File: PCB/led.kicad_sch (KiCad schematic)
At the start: 200 parts

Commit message: LED Diode Placement finished
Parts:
- C10, C100, C101, C102, C103, C104, C105, C106, C107, C108, C11, C12, C13, C14, C15, C16, C17, C18, C19, C20, C21, C22, C23, C24, C25, C26, C27, C28, C29, C30, C31, C32, C33, C34, C35, C36, C37, C38, C39, C40, C41, C42, C43, C44, C45, C46, C47, C48, C49, C50, C51, C52, C53, C54, C55, C56, C57, C58, C59, C60, C61, C62, C63, C64, C65, C66, C67, C68, C69, C70, C71, C72, C73, C74, C75, C76, C77, C78, C79, C80, C81, C82, C83, C84, C85, C86, C87, C88, C89, C9, C90, C91, C92, C93, C94, C95, C96, C97, C98, C99: footprint Capacitor_SMD:C_0805_2012Metric -> (none)

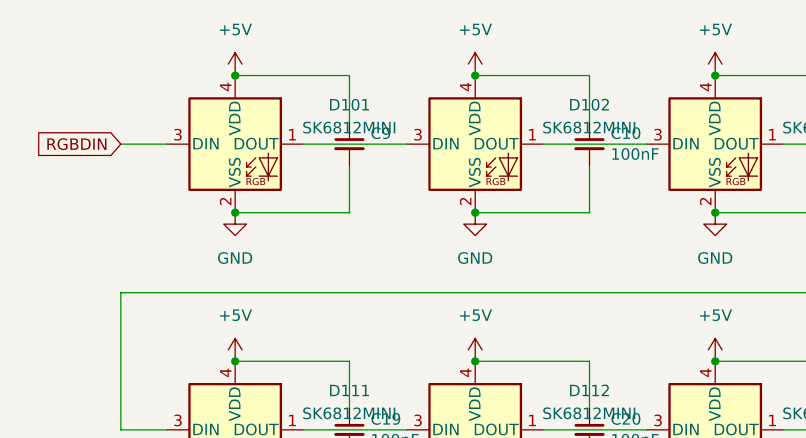
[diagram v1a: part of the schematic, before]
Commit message: LED +5 Wired, COL and ROW Buses nearly finished
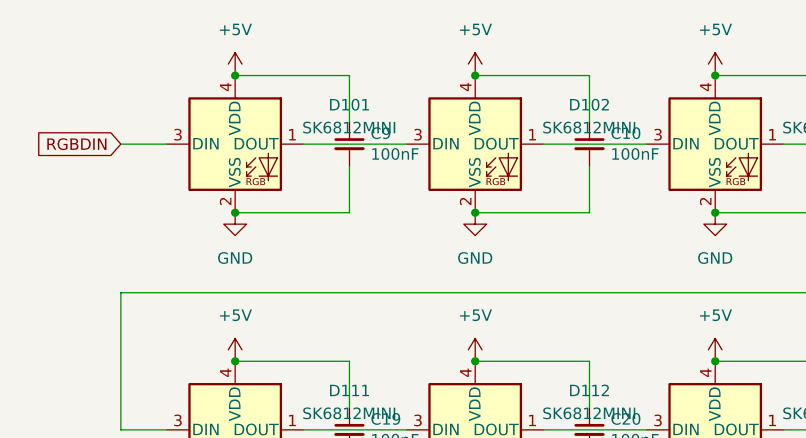
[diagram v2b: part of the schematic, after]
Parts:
- C10, C100, C101, C102, C103, C104, C105, C106, C107, C108, C11, C12, C13, C14, C15, C16, C17, C18, C19, C20, C21, C22, C23, C24, C25, C26, C27, C28, C29, C30, C31, C32, C33, C34, C35, C36, C37, C38, C39, C40, C41, C42, C43, C44, C45, C46, C47, C48, C49, C50, C51, C52, C53, C54, C55, C56, C57, C58, C59, C60, C61, C62, C63, C64, C65, C66, C67, C68, C69, C70, C71, C72, C73, C74, C75, C76, C77, C78, C79, C80, C81, C82, C83, C84, C85, C86, C87, C88, C89, C90, C91, C92, C93, C94, C95, C96, C97, C98, C99: footprint (none) -> led:led_capacitor
- C9: value (none) -> 100nF; footprint (none) -> led:led_capacitor

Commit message: datalines and mosfet
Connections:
- net +5V: no longer C10.1, C11.1, C12.1, C13.1, C14.1, C15.1, C16.1, C17.1, C18.1, C9.1, D101.4 (VDD), D102.4 (VDD), D103.4 (VDD), D104.4 (VDD), D105.4 (VDD), D106.4 (VDD), D107.4 (VDD), D108.4 (VDD), D109.4 (VDD), D110.4 (VDD)
- new net led_5V: C10.1, C11.1, C12.1, C13.1, C14.1, C15.1, C16.1, C17.1, C18.1, C9.1, D101.4 (VDD), D102.4 (VDD), D103.4 (VDD), D104.4 (VDD), D105.4 (VDD), D106.4 (VDD), D107.4 (VDD), D108.4 (VDD), D109.4 (VDD), D110.4 (VDD)

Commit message: Relocated JST Connector
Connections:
- net +5V is gone; now on net led_5V: C100.1, C101.1, C102.1, C103.1, C104.1, C105.1, C106.1, C107.1, C108.1, C19.1, C20.1, C21.1, C22.1, C23.1, C24.1, C25.1, C26.1, C27.1, C28.1, C29.1, C30.1, C31.1, C32.1, C33.1, C34.1, C35.1, C36.1, C37.1, C38.1, C39.1, C40.1, C41.1, C42.1, C43.1, C44.1, C45.1, C46.1, C47.1, C48.1, C49.1, C50.1, C51.1, C52.1, C53.1, C54.1, C55.1, C56.1, C57.1, C58.1, C59.1, C60.1, C61.1, C62.1, C63.1, C64.1, C65.1, C66.1, C67.1, C68.1, C69.1, C70.1, C71.1, C72.1, C73.1, C74.1, C75.1, C76.1, C77.1, C78.1, C79.1, C80.1, C81.1, C82.1, C83.1, C84.1, C85.1, C86.1, C87.1, C88.1, C89.1, C90.1, C91.1, C92.1, C93.1, C94.1, C95.1, C96.1, C97.1, C98.1, C99.1, D111.4 (VDD), D112.4 (VDD), D113.4 (VDD), D114.4 (VDD), D115.4 (VDD), D116.4 (VDD), D117.4 (VDD), D118.4 (VDD), D119.4 (VDD), D120.4 (VDD), D121.4 (VDD), D122.4 (VDD), D123.4 (VDD), D124.4 (VDD), D125.4 (VDD), D126.4 (VDD), D127.4 (VDD), D128.4 (VDD), D129.4 (VDD), D130.4 (VDD), D131.4 (VDD), D132.4 (VDD), D133.4 (VDD), D134.4 (VDD), D135.4 (VDD), D136.4 (VDD), D137.4 (VDD), D138.4 (VDD), D139.4 (VDD), D140.4 (VDD), D141.4 (VDD), D142.4 (VDD), D143.4 (VDD), D144.4 (VDD), D145.4 (VDD), D146.4 (VDD), D147.4 (VDD), D148.4 (VDD), D149.4 (VDD), D150.4 (VDD), D151.4 (VDD), D152.4 (VDD), D153.4 (VDD), D154.4 (VDD), D155.4 (VDD), D156.4 (VDD), D157.4 (VDD), D158.4 (VDD), D159.4 (VDD), D160.4 (VDD), D161.4 (VDD), D162.4 (VDD), D163.4 (VDD), D164.4 (VDD), D165.4 (VDD), D166.4 (VDD), D167.4 (VDD), D168.4 (VDD), D169.4 (VDD), D170.4 (VDD), D171.4 (VDD), D172.4 (VDD), D173.4 (VDD), D174.4 (VDD), D175.4 (VDD), D176.4 (VDD), D177.4 (VDD), D178.4 (VDD), D179.4 (VDD), D180.4 (VDD), D181.4 (VDD), D182.4 (VDD), D183.4 (VDD), D184.4 (VDD), D185.4 (VDD), D186.4 (VDD), D187.4 (VDD), D188.4 (VDD), D189.4 (VDD), D190.4 (VDD), D191.4 (VDD), D192.4 (VDD), D193.4 (VDD), D194.4 (VDD), D195.4 (VDD), D196.4 (VDD), D197.4 (VDD), D198.4 (VDD), D199.4 (VDD), D200.4 (VDD)

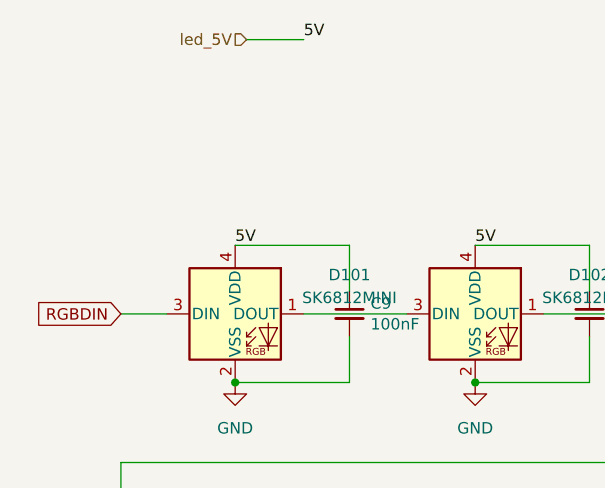
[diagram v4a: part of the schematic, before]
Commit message: change port position
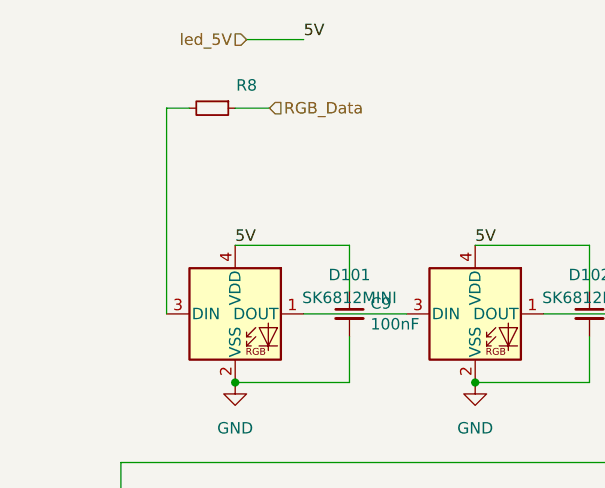
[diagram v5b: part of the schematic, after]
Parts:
- added R8: (no value), symbol Device:R_Small
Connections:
- net RGBDIN: no longer names the net of D101.3 (DIN)
- net RGBDIN: now also R8.2
- new net RGB_Data: R8.1
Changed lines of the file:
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@@
     (stroke (width 0) (type default) (color 0 0 0 0))
   )
+  (wire (pts (xy 17.78 59.69) (xy 17.78 36.83))
+    (stroke (width 0) (type default) (color 0 0 0 0))
+  )
   (wire (pts (xy 144.78 147.32) (xy 144.78 152.4))
     (stroke (width 0) (type default) (color 0 0 0 0))
@@
     (stroke (width 0) (type default) (color 0 0 0 0))
   )
-  (wire (pts (xy 12.7 59.69) (xy 17.78 59.69))
-    (stroke (width 0) (type default) (color 0 0 0 0))
-  )
   (wire (pts (xy 25.4 321.31) (xy 38.1 321.31))
     (stroke (width 0) (type default) (color 0 0 0 0))
@@
     (stroke (width 0) (type default) (color 0 0 0 0))
   )
+  (wire (pts (xy 25.4 36.83) (xy 29.21 36.83))
+    (stroke (width 0) (type default) (color 0 0 0 0))
+  )
   (wire (pts (xy 273.05 218.44) (xy 284.48 218.44))
     (stroke (width 0) (type default) (color 0 0 0 0))
@@
     (stroke (width 0) (type default) (color 0 0 0 0))
   )
+  (wire (pts (xy 17.78 36.83) (xy 20.32 36.83))
+    (stroke (width 0) (type default) (color 0 0 0 0))
+  )
   (wire (pts (xy 118.11 52.07) (xy 118.11 57.15))
     (stroke (width 0) (type default) (color 0 0 0 0))
@@
     (effects (font (size 1.27 1.27)) (justify left bottom))
   )
-  (global_label "RGBDIN" (shape input) (at 12.7 59.69 180) (fields_autoplaced)
-    (effects (font (size 1.27 1.27)) (justify right))
-    (property "Intersheet References" "${INTERSHEET_REFS}" (id 0) (at 3.3606 59.6106 0)
-      (effects (font (size 1.27 1.27)) (justify right) hide)
-    )
-  )
   (hierarchical_label "led_5V" (shape input) (at 26.67 29.21 180)
     (effects (font (size 1.27 1.27)) (justify right))
   )
+  (hierarchical_label "RGB_Data" (shape input) (at 29.21 36.83 0)
+    (effects (font (size 1.27 1.27)) (justify left))
+  )
   (symbol (lib_id "power:GND") (at 25.4 289.56 0) (unit 1)
     (in_bom yes) (on_board yes) (fields_autoplaced)
@@
     (pin "1")
   )
+  (symbol (lib_id "Device:R_Small") (at 22.86 36.83 270) (unit 1)
+    (in_bom yes) (on_board yes)
+    (property "Reference" "R8" (id 0) (at 26.67 34.29 90))
+    (property "Value" "" (id 1) (at 22.86 34.163 90))
+    (property "Footprint" "" (id 2) (at 22.86 36.83 0)
+      (effects (font (size 1.27 1.27)) hide)
+    )
+    (property "Datasheet" "~" (id 3) (at 22.86 36.83 0)
+      (effects (font (size 1.27 1.27)) hide)
+    )
+    (pin "1")
+    (pin "2")
+  )
   (symbol (lib_id "Device:C_Small") (at 118.11 123.19 0) (unit 1)

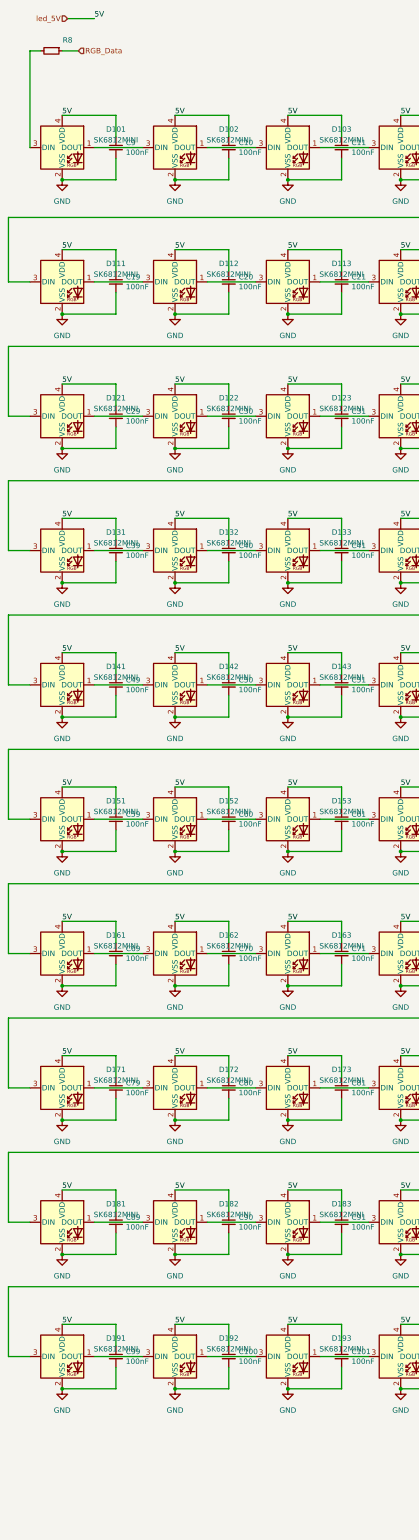
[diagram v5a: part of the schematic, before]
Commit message: changes:\n\n -change zones\n -add mounting holes\n -change via size
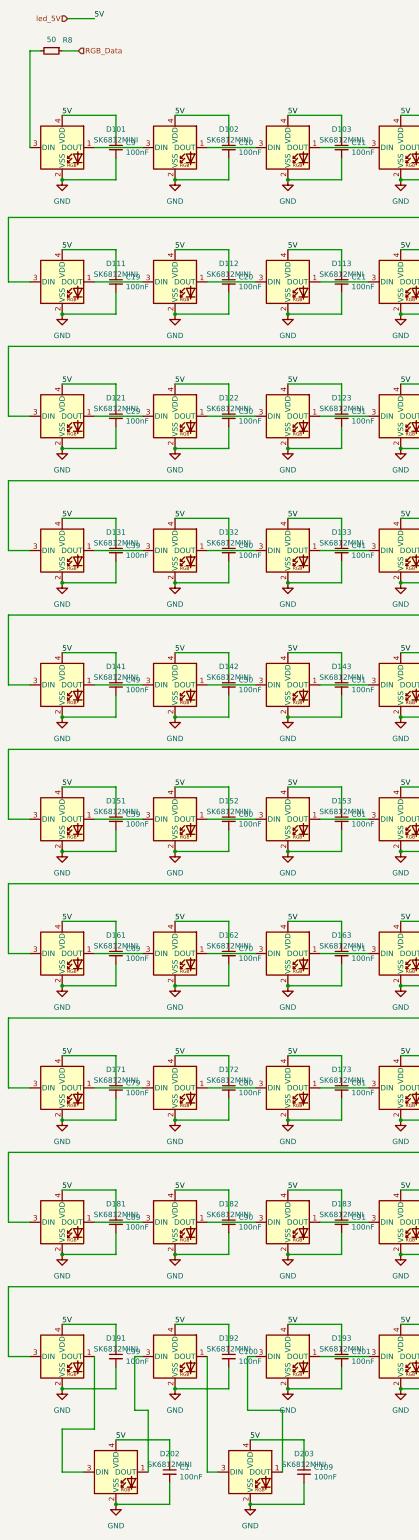
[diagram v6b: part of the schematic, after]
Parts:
- added C1, C109: 100nF, led:led_capacitor, symbol Device:C_Small
- added D202, D203: SK6812MINI, led:SK6812MINI_3.5x3.7mm_SMD-Flipped-Back, symbol LED:SK6812MINI
- R8: value (none) -> 50; footprint (none) -> Resistor_SMD:R_0805_2012Metric
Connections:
- net GND: now also C1.2, C109.2, D202.2 (VSS), D203.2 (VSS)
- net led_5V: now also C1.1, C109.1, D202.4 (VDD), D203.4 (VDD)
- net at D193.3 (DIN): now also D203.1 (DOUT); no longer D192.1 (DOUT)
- net at D192.3 (DIN): now also D202.1 (DOUT); no longer D191.1 (DOUT)
- new net: D192.1 (DOUT), D203.3 (DIN)
- new net: D191.1 (DOUT), D202.3 (DIN)

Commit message: production?
still hope
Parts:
- C1, C10, C100, C101, C102, C103, C104, C105, C106, C107, C108, C109, C11, C12, C13, C14, C15, C16, C17, C18, C19, C20, C21, C22, C23, C24, C25, C26, C27, C28, C29, C30, C31, C32, C33, C34, C35, C36, C37, C38, C39, C40, C41, C42, C43, C44, C45, C46, C47, C48, C49, C50, C51, C52, C53, C54, C55, C56, C57, C58, C59, C60, C61, C62, C63, C64, C65, C66, C67, C68, C69, C70, C71, C72, C73, C74, C75, C76, C77, C78, C79, C80, C81, C82, C83, C84, C85, C86, C87, C88, C89, C9, C90, C91, C92, C93, C94, C95, C96, C97, C98, C99: LCSC Part (none) -> C476766
- D101, D102, D103, D104, D105, D106, D107, D108, D109, D110, D111, D112, D113, D114, D115, D116, D117, D118, D119, D120, D121, D122, D123, D124, D125, D126, D127, D128, D129, D130, D131, D132, D133, D134, D135, D136, D137, D138, D139, D140, D141, D142, D143, D144, D145, D146, D147, D148, D149, D150, D151, D152, D153, D154, D155, D156, D157, D158, D159, D160, D161, D162, D163, D164, D165, D166, D167, D168, D169, D170, D171, D172, D173, D174, D175, D176, D177, D178, D179, D180, D181, D182, D183, D184, D185, D186, D187, D188, D189, D190, D191, D192, D193, D194, D195, D196, D197, D198, D199, D200, D202, D203: footprint led:SK6812MINI_3.5x3.7mm_SMD-Flipped-Back -> (none)

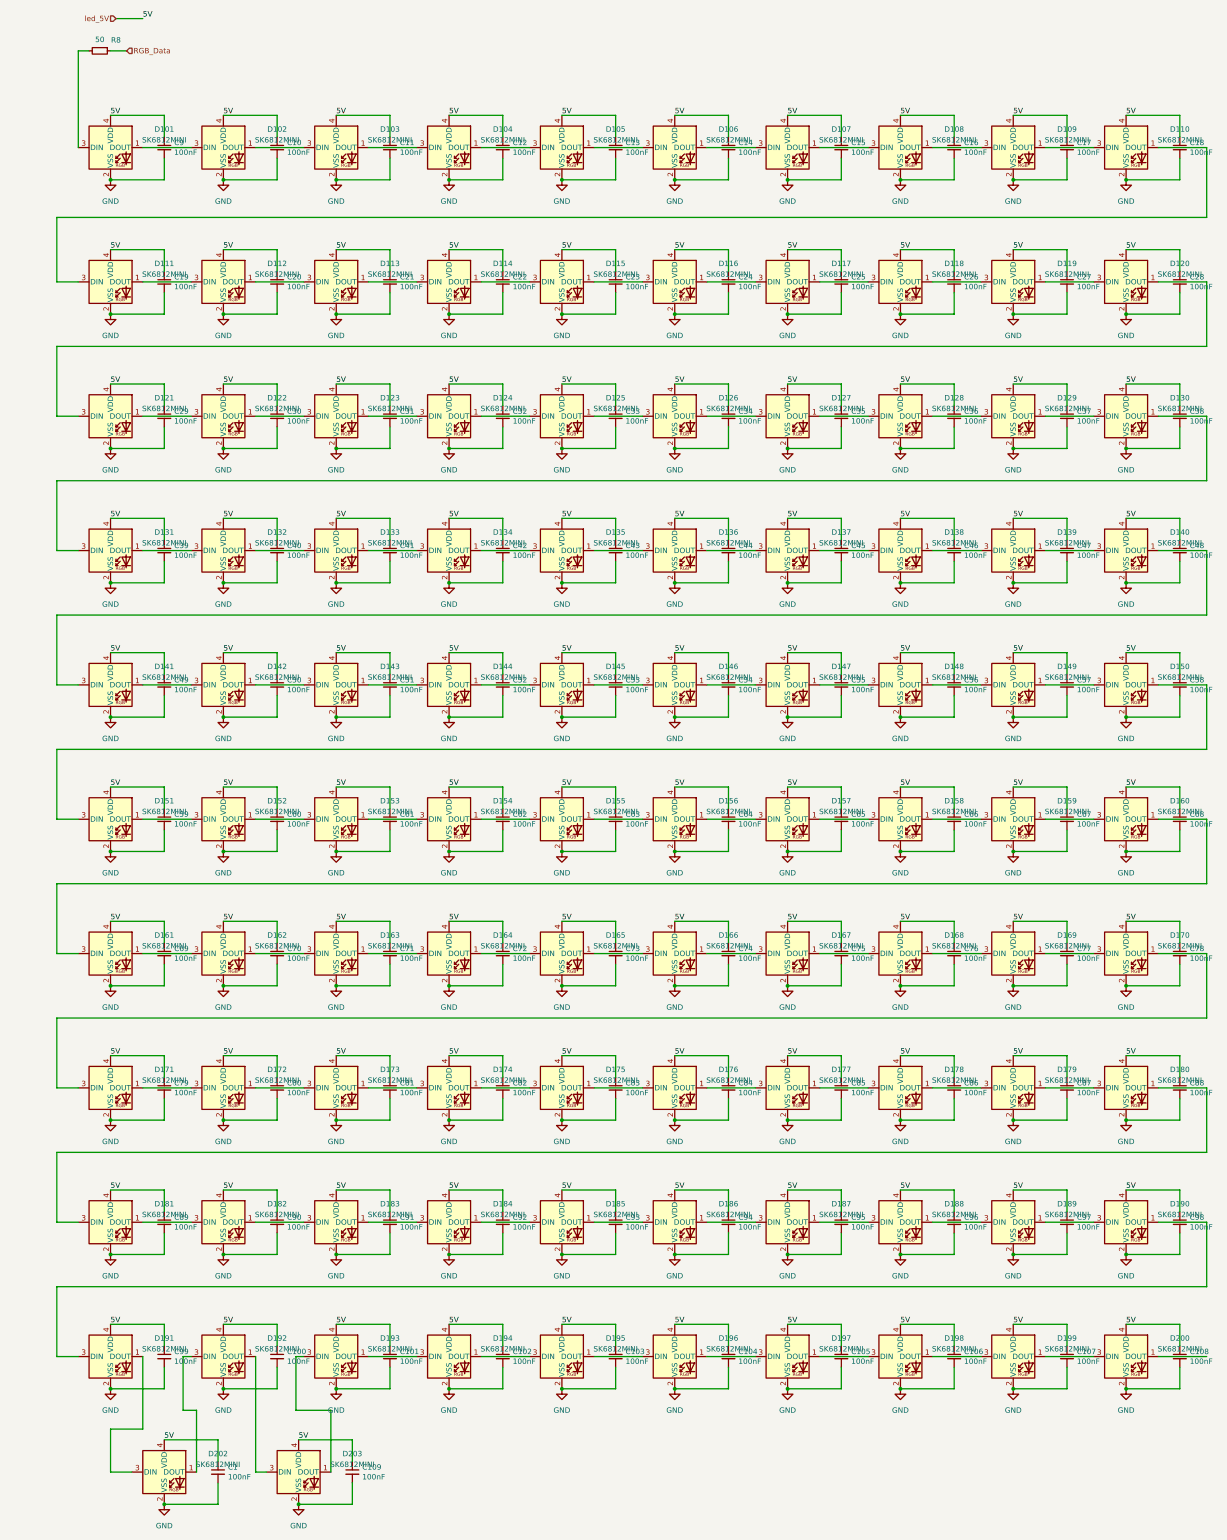
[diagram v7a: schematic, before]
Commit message: Fixed LEDs
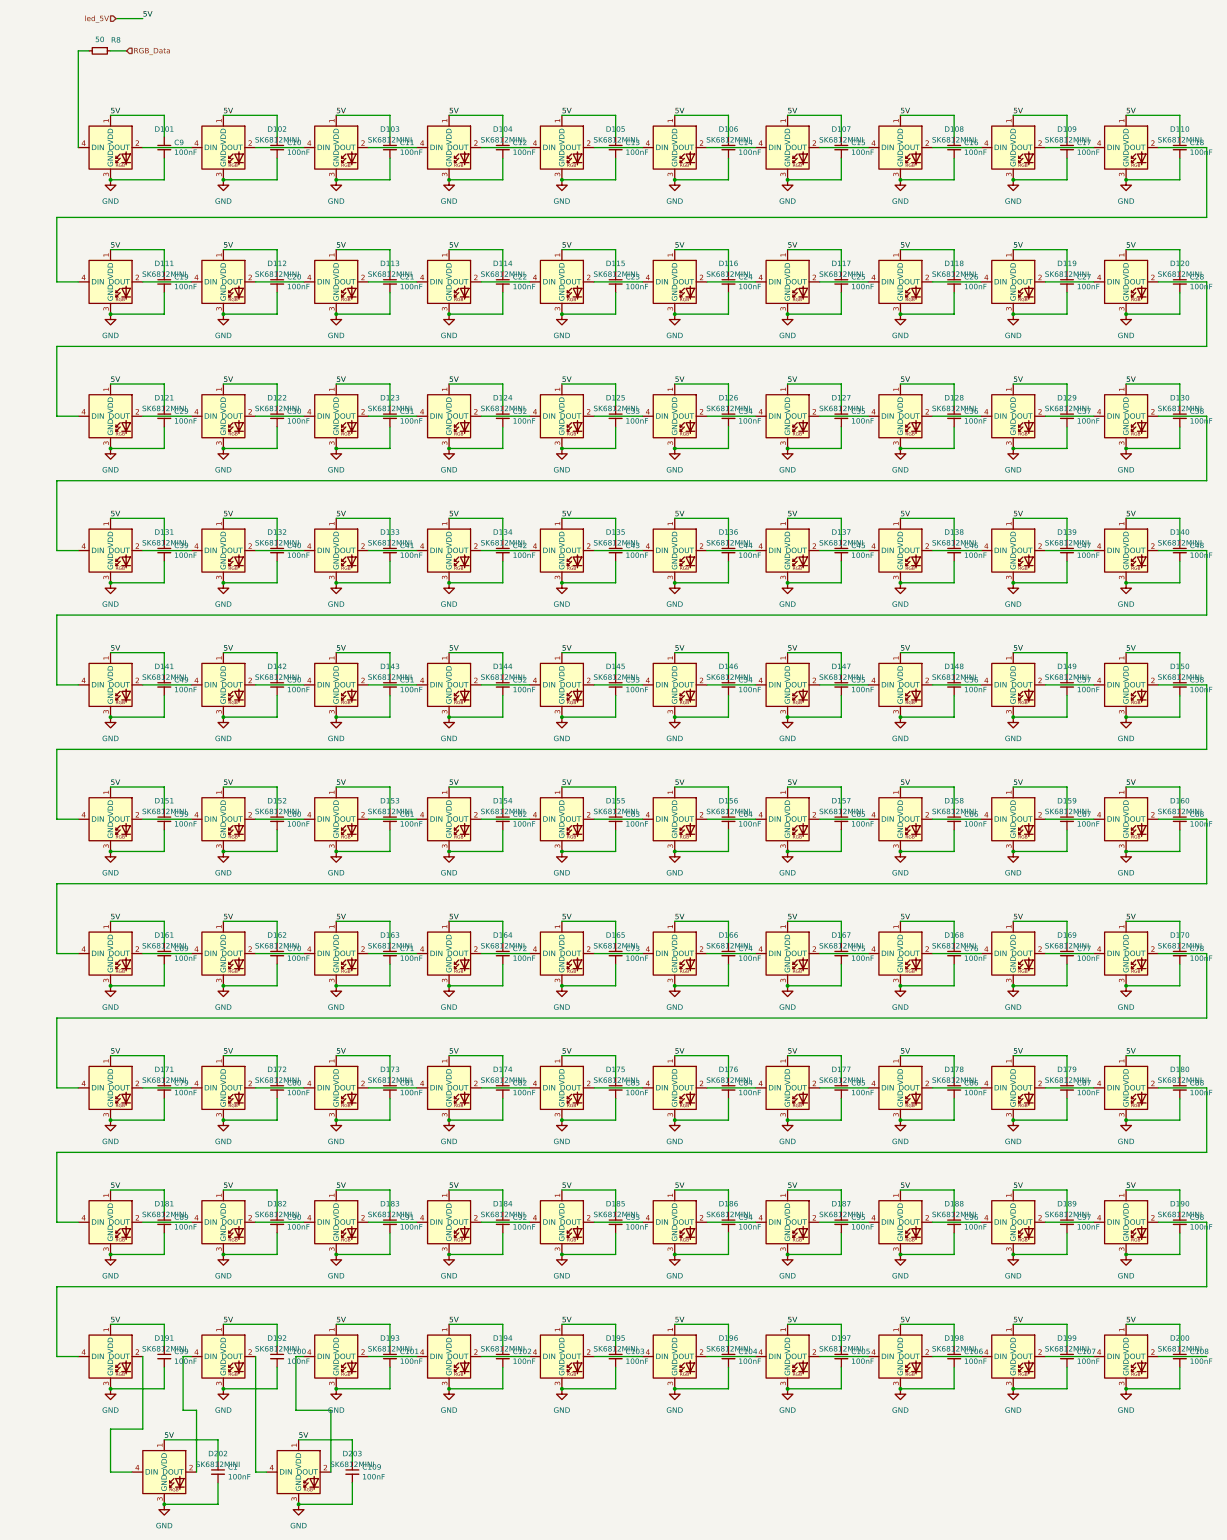
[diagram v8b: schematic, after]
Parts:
- D101: value SK6812MINI -> (none); symbol LED:SK6812MINI -> randomSymbols:SK6812MINI-E
- D102, D103, D104, D105, D106, D107, D108, D109, D110, D111, D112, D113, D114, D115, D116, D117, D118, D119, D120, D121, D122, D123, D124, D125, D126, D127, D128, D129, D130, D131, D132, D133, D134, D135, D136, D137, D138, D139, D140, D141, D142, D143, D144, D145, D146, D147, D148, D149, D150, D151, D152, D153, D154, D155, D156, D157, D158, D159, D160, D161, D162, D163, D164, D165, D166, D167, D168, D169, D170, D171, D172, D173, D174, D175, D176, D177, D178, D179, D180, D181, D182, D183, D184, D185, D186, D187, D188, D189, D190, D191, D192, D193, D194, D195, D196, D197, D198, D199, D200, D202, D203: symbol LED:SK6812MINI -> randomSymbols:SK6812MINI-E
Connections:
- net GND: now also D101.3 (GND), D102.3 (GND), D103.3 (GND), D104.3 (GND), D105.3 (GND), D106.3 (GND), D107.3 (GND), D108.3 (GND), D109.3 (GND), D110.3 (GND), D111.3 (GND), D112.3 (GND), D113.3 (GND), D114.3 (GND), D115.3 (GND), D116.3 (GND), D117.3 (GND), D118.3 (GND), D119.3 (GND), D120.3 (GND), D121.3 (GND), D122.3 (GND), D123.3 (GND), D124.3 (GND), D125.3 (GND), D126.3 (GND), D127.3 (GND), D128.3 (GND), D129.3 (GND), D130.3 (GND), D131.3 (GND), D132.3 (GND), D133.3 (GND), D134.3 (GND), D135.3 (GND), D136.3 (GND), D137.3 (GND), D138.3 (GND), D139.3 (GND), D140.3 (GND), D141.3 (GND), D142.3 (GND), D143.3 (GND), D144.3 (GND), D145.3 (GND), D146.3 (GND), D147.3 (GND), D148.3 (GND), D149.3 (GND), D150.3 (GND), D151.3 (GND), D152.3 (GND), D153.3 (GND), D154.3 (GND), D155.3 (GND), D156.3 (GND), D157.3 (GND), D158.3 (GND), D159.3 (GND), D160.3 (GND), D161.3 (GND), D162.3 (GND), D163.3 (GND), D164.3 (GND), D165.3 (GND), D166.3 (GND), D167.3 (GND), D168.3 (GND), D169.3 (GND), D170.3 (GND), D171.3 (GND), D172.3 (GND), D173.3 (GND), D174.3 (GND), D175.3 (GND), D176.3 (GND), D177.3 (GND), D178.3 (GND), D179.3 (GND), D180.3 (GND), D181.3 (GND), D182.3 (GND), D183.3 (GND), D184.3 (GND), D185.3 (GND), D186.3 (GND), D187.3 (GND), D188.3 (GND), D189.3 (GND), D190.3 (GND), D191.3 (GND), D192.3 (GND), D193.3 (GND), D194.3 (GND), D195.3 (GND), D196.3 (GND), D197.3 (GND), D198.3 (GND), D199.3 (GND), D200.3 (GND), D202.3 (GND), D203.3 (GND); no longer D101.2 (VSS), D102.2 (VSS), D103.2 (VSS), D104.2 (VSS), D105.2 (VSS), D106.2 (VSS), D107.2 (VSS), D108.2 (VSS), D109.2 (VSS), D110.2 (VSS), D111.2 (VSS), D112.2 (VSS), D113.2 (VSS), D114.2 (VSS), D115.2 (VSS), D116.2 (VSS), D117.2 (VSS), D118.2 (VSS), D119.2 (VSS), D120.2 (VSS), D121.2 (VSS), D122.2 (VSS), D123.2 (VSS), D124.2 (VSS), D125.2 (VSS), D126.2 (VSS), D127.2 (VSS), D128.2 (VSS), D129.2 (VSS), D130.2 (VSS), D131.2 (VSS), D132.2 (VSS), D133.2 (VSS), D134.2 (VSS), D135.2 (VSS), D136.2 (VSS), D137.2 (VSS), D138.2 (VSS), D139.2 (VSS), D140.2 (VSS), D141.2 (VSS), D142.2 (VSS), D143.2 (VSS), D144.2 (VSS), D145.2 (VSS), D146.2 (VSS), D147.2 (VSS), D148.2 (VSS), D149.2 (VSS), D150.2 (VSS), D151.2 (VSS), D152.2 (VSS), D153.2 (VSS), D154.2 (VSS), D155.2 (VSS), D156.2 (VSS), D157.2 (VSS), D158.2 (VSS), D159.2 (VSS), D160.2 (VSS), D161.2 (VSS), D162.2 (VSS), D163.2 (VSS), D164.2 (VSS), D165.2 (VSS), D166.2 (VSS), D167.2 (VSS), D168.2 (VSS), D169.2 (VSS), D170.2 (VSS), D171.2 (VSS), D172.2 (VSS), D173.2 (VSS), D174.2 (VSS), D175.2 (VSS), D176.2 (VSS), D177.2 (VSS), D178.2 (VSS), D179.2 (VSS), D180.2 (VSS), D181.2 (VSS), D182.2 (VSS), D183.2 (VSS), D184.2 (VSS), D185.2 (VSS), D186.2 (VSS), D187.2 (VSS), D188.2 (VSS), D189.2 (VSS), D190.2 (VSS), D191.2 (VSS), D192.2 (VSS), D193.2 (VSS), D194.2 (VSS), D195.2 (VSS), D196.2 (VSS), D197.2 (VSS), D198.2 (VSS), D199.2 (VSS), D200.2 (VSS), D202.2 (VSS), D203.2 (VSS)
- net led_5V: now also D101.1 (VDD), D102.1 (VDD), D103.1 (VDD), D104.1 (VDD), D105.1 (VDD), D106.1 (VDD), D107.1 (VDD), D108.1 (VDD), D109.1 (VDD), D110.1 (VDD), D111.1 (VDD), D112.1 (VDD), D113.1 (VDD), D114.1 (VDD), D115.1 (VDD), D116.1 (VDD), D117.1 (VDD), D118.1 (VDD), D119.1 (VDD), D120.1 (VDD), D121.1 (VDD), D122.1 (VDD), D123.1 (VDD), D124.1 (VDD), D125.1 (VDD), D126.1 (VDD), D127.1 (VDD), D128.1 (VDD), D129.1 (VDD), D130.1 (VDD), D131.1 (VDD), D132.1 (VDD), D133.1 (VDD), D134.1 (VDD), D135.1 (VDD), D136.1 (VDD), D137.1 (VDD), D138.1 (VDD), D139.1 (VDD), D140.1 (VDD), D141.1 (VDD), D142.1 (VDD), D143.1 (VDD), D144.1 (VDD), D145.1 (VDD), D146.1 (VDD), D147.1 (VDD), D148.1 (VDD), D149.1 (VDD), D150.1 (VDD), D151.1 (VDD), D152.1 (VDD), D153.1 (VDD), D154.1 (VDD), D155.1 (VDD), D156.1 (VDD), D157.1 (VDD), D158.1 (VDD), D159.1 (VDD), D160.1 (VDD), D161.1 (VDD), D162.1 (VDD), D163.1 (VDD), D164.1 (VDD), D165.1 (VDD), D166.1 (VDD), D167.1 (VDD), D168.1 (VDD), D169.1 (VDD), D170.1 (VDD), D171.1 (VDD), D172.1 (VDD), D173.1 (VDD), D174.1 (VDD), D175.1 (VDD), D176.1 (VDD), D177.1 (VDD), D178.1 (VDD), D179.1 (VDD), D180.1 (VDD), D181.1 (VDD), D182.1 (VDD), D183.1 (VDD), D184.1 (VDD), D185.1 (VDD), D186.1 (VDD), D187.1 (VDD), D188.1 (VDD), D189.1 (VDD), D190.1 (VDD), D191.1 (VDD), D192.1 (VDD), D193.1 (VDD), D194.1 (VDD), D195.1 (VDD), D196.1 (VDD), D197.1 (VDD), D198.1 (VDD), D199.1 (VDD), D200.1 (VDD), D202.1 (VDD), D203.1 (VDD); no longer D101.4 (VDD), D102.4 (VDD), D103.4 (VDD), D104.4 (VDD), D105.4 (VDD), D106.4 (VDD), D107.4 (VDD), D108.4 (VDD), D109.4 (VDD), D110.4 (VDD), D111.4 (VDD), D112.4 (VDD), D113.4 (VDD), D114.4 (VDD), D115.4 (VDD), D116.4 (VDD), D117.4 (VDD), D118.4 (VDD), D119.4 (VDD), D120.4 (VDD), D121.4 (VDD), D122.4 (VDD), D123.4 (VDD), D124.4 (VDD), D125.4 (VDD), D126.4 (VDD), D127.4 (VDD), D128.4 (VDD), D129.4 (VDD), D130.4 (VDD), D131.4 (VDD), D132.4 (VDD), D133.4 (VDD), D134.4 (VDD), D135.4 (VDD), D136.4 (VDD), D137.4 (VDD), D138.4 (VDD), D139.4 (VDD), D140.4 (VDD), D141.4 (VDD), D142.4 (VDD), D143.4 (VDD), D144.4 (VDD), D145.4 (VDD), D146.4 (VDD), D147.4 (VDD), D148.4 (VDD), D149.4 (VDD), D150.4 (VDD), D151.4 (VDD), D152.4 (VDD), D153.4 (VDD), D154.4 (VDD), D155.4 (VDD), D156.4 (VDD), D157.4 (VDD), D158.4 (VDD), D159.4 (VDD), D160.4 (VDD), D161.4 (VDD), D162.4 (VDD), D163.4 (VDD), D164.4 (VDD), D165.4 (VDD), D166.4 (VDD), D167.4 (VDD), D168.4 (VDD), D169.4 (VDD), D170.4 (VDD), D171.4 (VDD), D172.4 (VDD), D173.4 (VDD), D174.4 (VDD), D175.4 (VDD), D176.4 (VDD), D177.4 (VDD), D178.4 (VDD), D179.4 (VDD), D180.4 (VDD), D181.4 (VDD), D182.4 (VDD), D183.4 (VDD), D184.4 (VDD), D185.4 (VDD), D186.4 (VDD), D187.4 (VDD), D188.4 (VDD), D189.4 (VDD), D190.4 (VDD), D191.4 (VDD), D192.4 (VDD), D193.4 (VDD), D194.4 (VDD), D195.4 (VDD), D196.4 (VDD), D197.4 (VDD), D198.4 (VDD), D199.4 (VDD), D200.4 (VDD), D202.4 (VDD), D203.4 (VDD)
- net at R8.2: now also D101.4 (DIN); no longer D101.3 (DIN)
- new net: D145.2 (DOUT), D146.4 (DIN)
- new net: D144.2 (DOUT), D145.4 (DIN)
- new net: D179.2 (DOUT), D180.4 (DIN)
- new net: D178.2 (DOUT), D179.4 (DIN)
- new net: D122.2 (DOUT), D123.4 (DIN)
- new net: D121.2 (DOUT), D122.4 (DIN)
- new net: D193.2 (DOUT), D194.4 (DIN)
- new net: D193.4 (DIN), D203.2 (DOUT)
- new net: D149.2 (DOUT), D150.4 (DIN)
- new net: D148.2 (DOUT), D149.4 (DIN)
- new net: D132.2 (DOUT), D133.4 (DIN)
- new net: D131.2 (DOUT), D132.4 (DIN)
- new net: D192.2 (DOUT), D203.4 (DIN)
- new net: D156.2 (DOUT), D157.4 (DIN)
- new net: D155.2 (DOUT), D156.4 (DIN)
- new net: D181.2 (DOUT), D182.4 (DIN)
- new net: D180.2 (DOUT), D181.4 (DIN)
- new net: D130.2 (DOUT), D131.4 (DIN)
- new net: D198.2 (DOUT), D199.4 (DIN)
- new net: D197.2 (DOUT), D198.4 (DIN)
- new net: D133.2 (DOUT), D134.4 (DIN)
- new net: D147.2 (DOUT), D148.4 (DIN)
- new net: D169.2 (DOUT), D170.4 (DIN)
- new net: D168.2 (DOUT), D169.4 (DIN)
- new net: D123.2 (DOUT), D124.4 (DIN)
- new net: D177.2 (DOUT), D178.4 (DIN)
- new net: D176.2 (DOUT), D177.4 (DIN)
- new net: D126.2 (DOUT), D127.4 (DIN)
- new net: D125.2 (DOUT), D126.4 (DIN)
- new net: D192.4 (DIN), D202.2 (DOUT)
- new net: D191.2 (DOUT), D202.4 (DIN)
- new net: D159.2 (DOUT), D160.4 (DIN)
- new net: D158.2 (DOUT), D159.4 (DIN)
- new net: D141.2 (DOUT), D142.4 (DIN)
- new net: D140.2 (DOUT), D141.4 (DIN)
- new net: D113.2 (DOUT), D114.4 (DIN)
- new net: D112.2 (DOUT), D113.4 (DIN)
- new net: D146.2 (DOUT), D147.4 (DIN)
- new net: D175.2 (DOUT), D176.4 (DIN)
- new net: D151.2 (DOUT), D152.4 (DIN)
- new net: D150.2 (DOUT), D151.4 (DIN)
- new net: D111.2 (DOUT), D112.4 (DIN)
- new net: D110.2 (DOUT), D111.4 (DIN)
- new net: D138.2 (DOUT), D139.4 (DIN)
- new net: D137.2 (DOUT), D138.4 (DIN)
- new net: D103.2 (DOUT), D104.4 (DIN)
- new net: D102.2 (DOUT), D103.4 (DIN)
- new net: D154.2 (DOUT), D155.4 (DIN)
- new net: D139.2 (DOUT), D140.4 (DIN)
- new net: D166.2 (DOUT), D167.4 (DIN)
- new net: D165.2 (DOUT), D166.4 (DIN)
- new net: D170.2 (DOUT), D171.4 (DIN)
- new net: D136.2 (DOUT), D137.4 (DIN)
- new net: D135.2 (DOUT), D136.4 (DIN)
- new net: D109.2 (DOUT), D110.4 (DIN)
- new net: D108.2 (DOUT), D109.4 (DIN)
- new net: D142.2 (DOUT), D143.4 (DIN)
- new net: D143.2 (DOUT), D144.4 (DIN)
- new net: D164.2 (DOUT), D165.4 (DIN)
- new net: D163.2 (DOUT), D164.4 (DIN)
- new net: D134.2 (DOUT), D135.4 (DIN)
- new net: D183.2 (DOUT), D184.4 (DIN)
- new net: D182.2 (DOUT), D183.4 (DIN)
- new net: D120.2 (DOUT), D121.4 (DIN)
- new net: D174.2 (DOUT), D175.4 (DIN)
- new net: D119.2 (DOUT), D120.4 (DIN)
- new net: D118.2 (DOUT), D119.4 (DIN)
- new net: D101.2 (DOUT), D102.4 (DIN)
- new net: D172.2 (DOUT), D173.4 (DIN)
- new net: D171.2 (DOUT), D172.4 (DIN)
- new net: D196.2 (DOUT), D197.4 (DIN)
- new net: D188.2 (DOUT), D189.4 (DIN)
- new net: D187.2 (DOUT), D188.4 (DIN)
- new net: D117.2 (DOUT), D118.4 (DIN)
- new net: D128.2 (DOUT), D129.4 (DIN)
- new net: D127.2 (DOUT), D128.4 (DIN)
- new net: D190.2 (DOUT), D191.4 (DIN)
- new net: D195.2 (DOUT), D196.4 (DIN)
- new net: D194.2 (DOUT), D195.4 (DIN)
- new net: D189.2 (DOUT), D190.4 (DIN)
- new net: D160.2 (DOUT), D161.4 (DIN)
- new net: D184.2 (DOUT), D185.4 (DIN)
- new net: D105.2 (DOUT), D106.4 (DIN)
- new net: D104.2 (DOUT), D105.4 (DIN)
- new net: D129.2 (DOUT), D130.4 (DIN)
- new net: D106.2 (DOUT), D107.4 (DIN)
- new net: D107.2 (DOUT), D108.4 (DIN)
- new net: D124.2 (DOUT), D125.4 (DIN)
- new net: D186.2 (DOUT), D187.4 (DIN)
- new net: D162.2 (DOUT), D163.4 (DIN)
- new net: D115.2 (DOUT), D116.4 (DIN)
- new net: D114.2 (DOUT), D115.4 (DIN)
- new net: D161.2 (DOUT), D162.4 (DIN)
- new net: D167.2 (DOUT), D168.4 (DIN)
- new net: D153.2 (DOUT), D154.4 (DIN)
- new net: D152.2 (DOUT), D153.4 (DIN)
- new net: D185.2 (DOUT), D186.4 (DIN)
- new net: D116.2 (DOUT), D117.4 (DIN)
- new net: D199.2 (DOUT), D200.4 (DIN)
- new net: D157.2 (DOUT), D158.4 (DIN)
- new net: D173.2 (DOUT), D174.4 (DIN)
